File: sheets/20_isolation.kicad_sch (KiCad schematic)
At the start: 0 parts

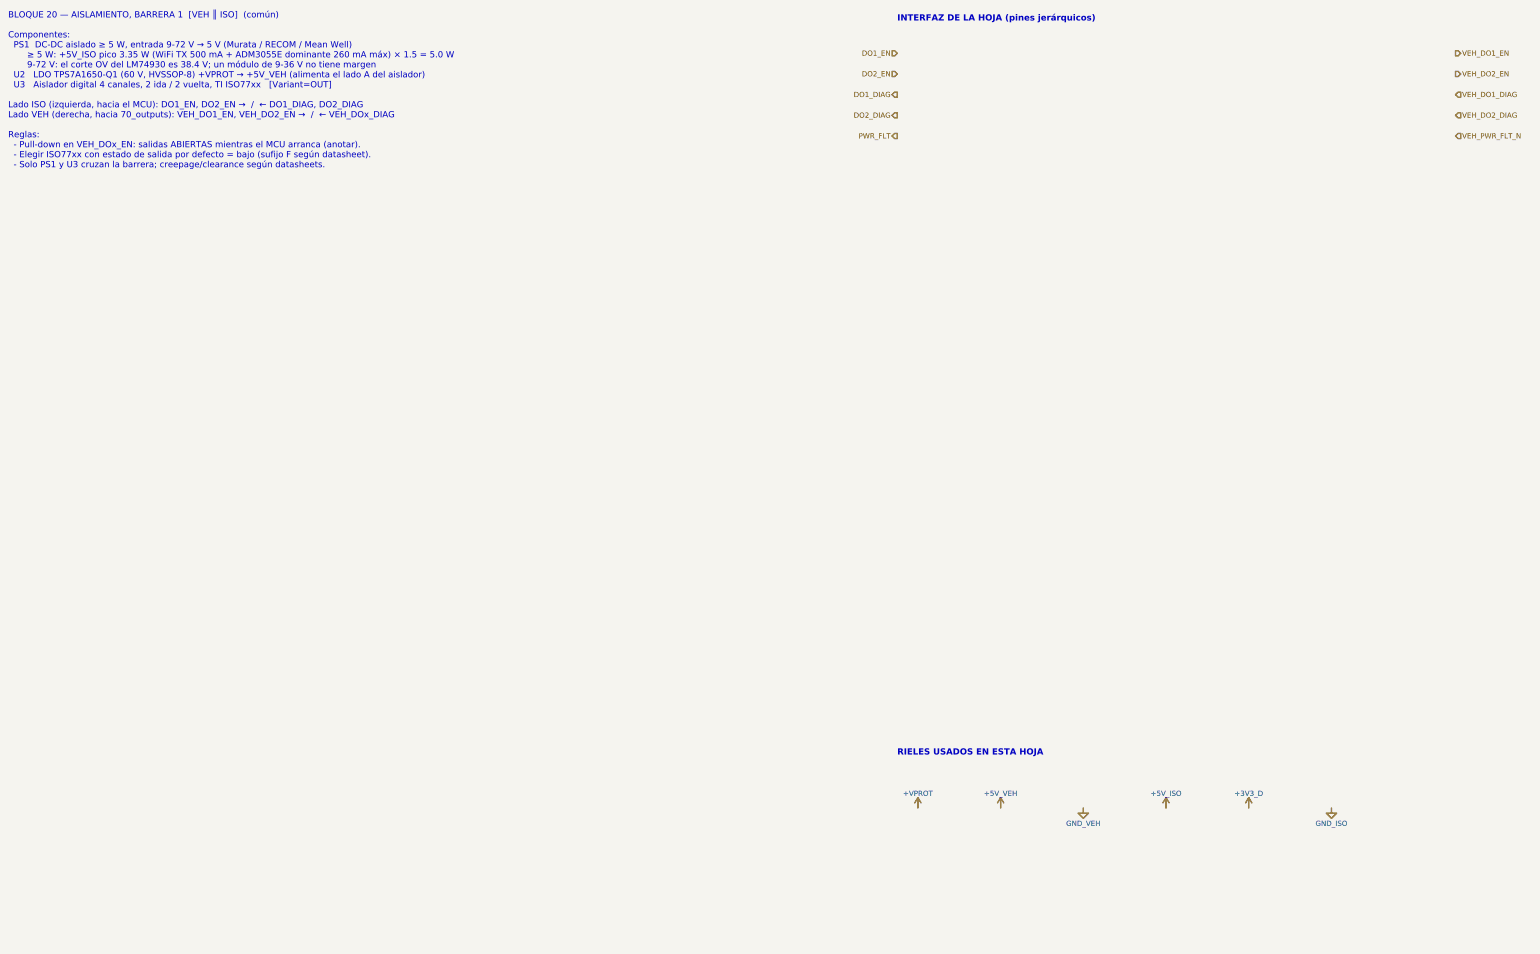
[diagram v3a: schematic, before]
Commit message: 20_isolation: PS201 EC4AW8-48S05, LDO +5V_VEH, ISO7763-Q1; PWR_FLT_N; L301 HandSolder
- Hoja 20 completa: PS201 Cincon EC4AW8-48S05 (sin Remote On/Off) con
  C201/C202/C203; U201 TPS7A1650-Q1 (+VPROT -> +5V_VEH; DELAY, PG y FB/NC
  abiertos según TI SBVS188E tabla 5-1); U202 ISO7763FQDWRQ1 con pull-downs
  R201-R204; notas de distancias de la barrera 1.
- Símbolo INCLI-VA:EC4AW8-48S05 creado desde la tabla de pines del datasheet
  Cincon V10 (excepción autorizada); huella oficial TRACO THD 15WIN verificada.
- Renombre PWR_FLT -> PWR_FLT_N en la raíz, 20 y 40_mcu.
- Huella INCLI-VA:L_Coilcraft_XAL4020_HandSolder (Coilcraft Doc 806-4,
  rev. 02/25/26) asignada a L301.
- Datasheets de EC4AW8 y XAL4020 en docs/datasheets.
- ERC: 0 en 20 y 30 (129 en el proyecto); sch_visual_qa PASS en 20.

Co-Authored-By: Claude Opus 5.5 <noreply@anthropic.com>
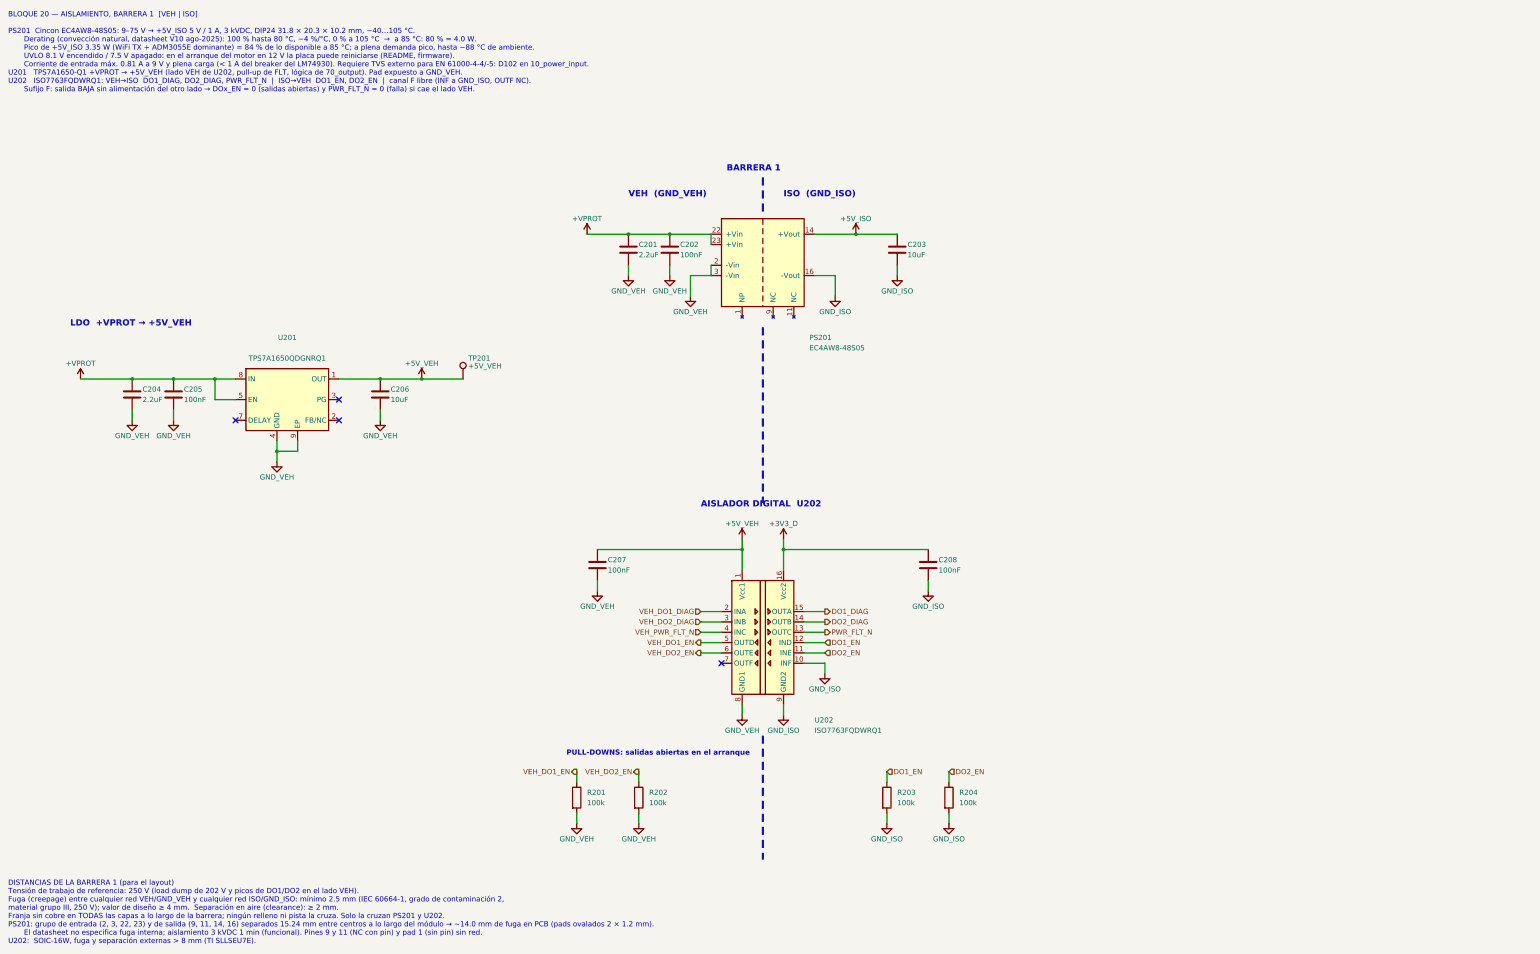
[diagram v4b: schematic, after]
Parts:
- added C201, C204: 2.2uF, Capacitor_SMD:C_1210_3225Metric, symbol Device:C
- added C202, C205, C207, C208: 100nF, Capacitor_SMD:C_0603_1608Metric, symbol Device:C
- added C203, C206: 10uF, Capacitor_SMD:C_0805_2012Metric, symbol Device:C
- added PS201: EC4AW8-48S05, Converter_DCDC:Converter_DCDC_TRACO_THD_15-xxxxWIN_THT, symbol INCLI-VA:EC4AW8-48S05
- added R201, R202, R203, R204: 100k, Resistor_SMD:R_0603_1608Metric, symbol Device:R
- added TP201: +5V_VEH, TestPoint:TestPoint_Pad_D1.5mm, symbol Connector:TestPoint
- added U201: TPS7A1650QDGNRQ1, Package_SO:HVSSOP-8-1EP_3x3mm_P0.65mm_EP1.57x1.89mm_ThermalVias, symbol easyeda2kicad:TPS7A1650QDGNRQ1
- added U202: ISO7763FQDWRQ1, Package_SO:SOIC-16W_7.5x10.3mm_P1.27mm, symbol Isolator:ISO7763FDW
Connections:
- net +3V3_D: now also C208.1, U202.16 (Vcc2)
- net +5V_ISO: now also C203.1, PS201.14 (+Vout)
- net +5V_VEH: now also C206.1, C207.1, TP201.1, U201.1 (OUT), U202.1 (Vcc1)
- net +VPROT: now also C201.1, C202.1, C204.1, C205.1, PS201.22 (+Vin), PS201.23 (+Vin), U201.5 (EN), U201.8 (IN)
- net DO1_DIAG: now also U202.15 (OUTA)
- net DO1_EN: now also R203.1, U202.12 (IND)
- net DO2_DIAG: now also U202.14 (OUTB)
- net DO2_EN: now also R204.1, U202.11 (INE)
- net GND_ISO: now also C203.2, C208.2, PS201.16 (-Vout), R203.2, R204.2, U202.10 (INF), U202.9 (GND2)
- net GND_VEH: now also C201.2, C202.2, C204.2, C205.2, C206.2, C207.2, PS201.2 (-Vin), PS201.3 (-Vin), R201.2, R202.2, U201.4 (GND), U201.9 (EP), U202.8 (GND1)
- net VEH_DO1_DIAG: now also U202.2 (INA)
- net VEH_DO1_EN: now also R201.1, U202.5 (OUTD)
- net VEH_DO2_DIAG: now also U202.3 (INB)
- net VEH_DO2_EN: now also R202.1, U202.6 (OUTE)
- net VEH_PWR_FLT_N: now also U202.4 (INC)
- new net PWR_FLT_N: U202.13 (OUTC)
- no-connect marks 0 -> 4
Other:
- note added: "AISLADOR DIGITAL U202"
- note added: "BARRERA 1"
- note added: "BLOQUE 20 — AISLAMIENTO, BARRERA 1 [VEH | ISO] PS201 Cincon EC4AW8-48S05: 9–75 V → +5V_ISO 5 V / 1 A, 3 kVDC, DIP24 31.8 × 20.3 × 10.2 mm, −40…105 °C. Derating (convección natural, datasheet V10 ago-2025): 100 % hasta 80 °C, −4 %/°C, 0 % a 105 °C → a 85 °C: 80 % = 4.0 W. Pico de +5V_ISO 3.35 W (WiFi TX + ADM3055E dominante) = 84 % de lo disponible a 85 °C; a plena demanda pico, hasta ~88 °C de am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"
- note added: "DISTANCIAS DE LA BARRERA 1 (para el layout) Tensión de trabajo de referencia: 250 V (load dump de 202 V y picos de DO1/DO2 en el lado VEH). Fuga (creepage) entre cualquier red VEH/GND_VEH y cualquier red ISO/GND_ISO: mínimo 2.5 mm (IEC 60664-1, grado de contaminación 2, material grupo III, 250 V); valor de diseño ≥ 4 mm. Separación en aire (clearance): ≥ 2 mm. Franja sin cobre en TODAS las capas 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"
- note added: "ISO (GND_ISO)"
- note added: "LDO +VPROT → +5V_VEH"
- note added: "PULL-DOWNS: salidas abiertas en el arranque"
- note added: "VEH (GND_VEH)"
- note removed: "BLOQUE 20 — AISLAMIENTO, BARRERA 1 [VEH ║ ISO] (común) Componentes: PS1 DC-DC aislado ≥ 5 W, entrada 9-72 V → 5 V (Murata / RECOM / Mean Well) ≥ 5 W: +5V_ISO pico 3.35 W (WiFi TX 500 mA + ADM3055E dominante 260 mA máx) × 1.5 = 5.0 W 9-72 V: el corte OV del LM74930 es 38.4 V; un módulo de 9-36 V no tiene margen U2 LDO TPS7A1650-Q1 (60 V, HVSSOP-8) +VPROT → +5V_VEH (alimenta el lado A del aislador)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"
- note removed: "INTERFAZ DE LA HOJA (pines jerárquicos)"
- note removed: "RIELES USADOS EN ESTA HOJA"
